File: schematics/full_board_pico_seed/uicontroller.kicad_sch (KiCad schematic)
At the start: 19 parts, among them J5 Conn_02x03_Odd_Even, SW1 Stompbutton 1, SW2 Stompbutton 2, SW3 Stompbutton 3, U5 ATmega88A-A, U6 24LC128

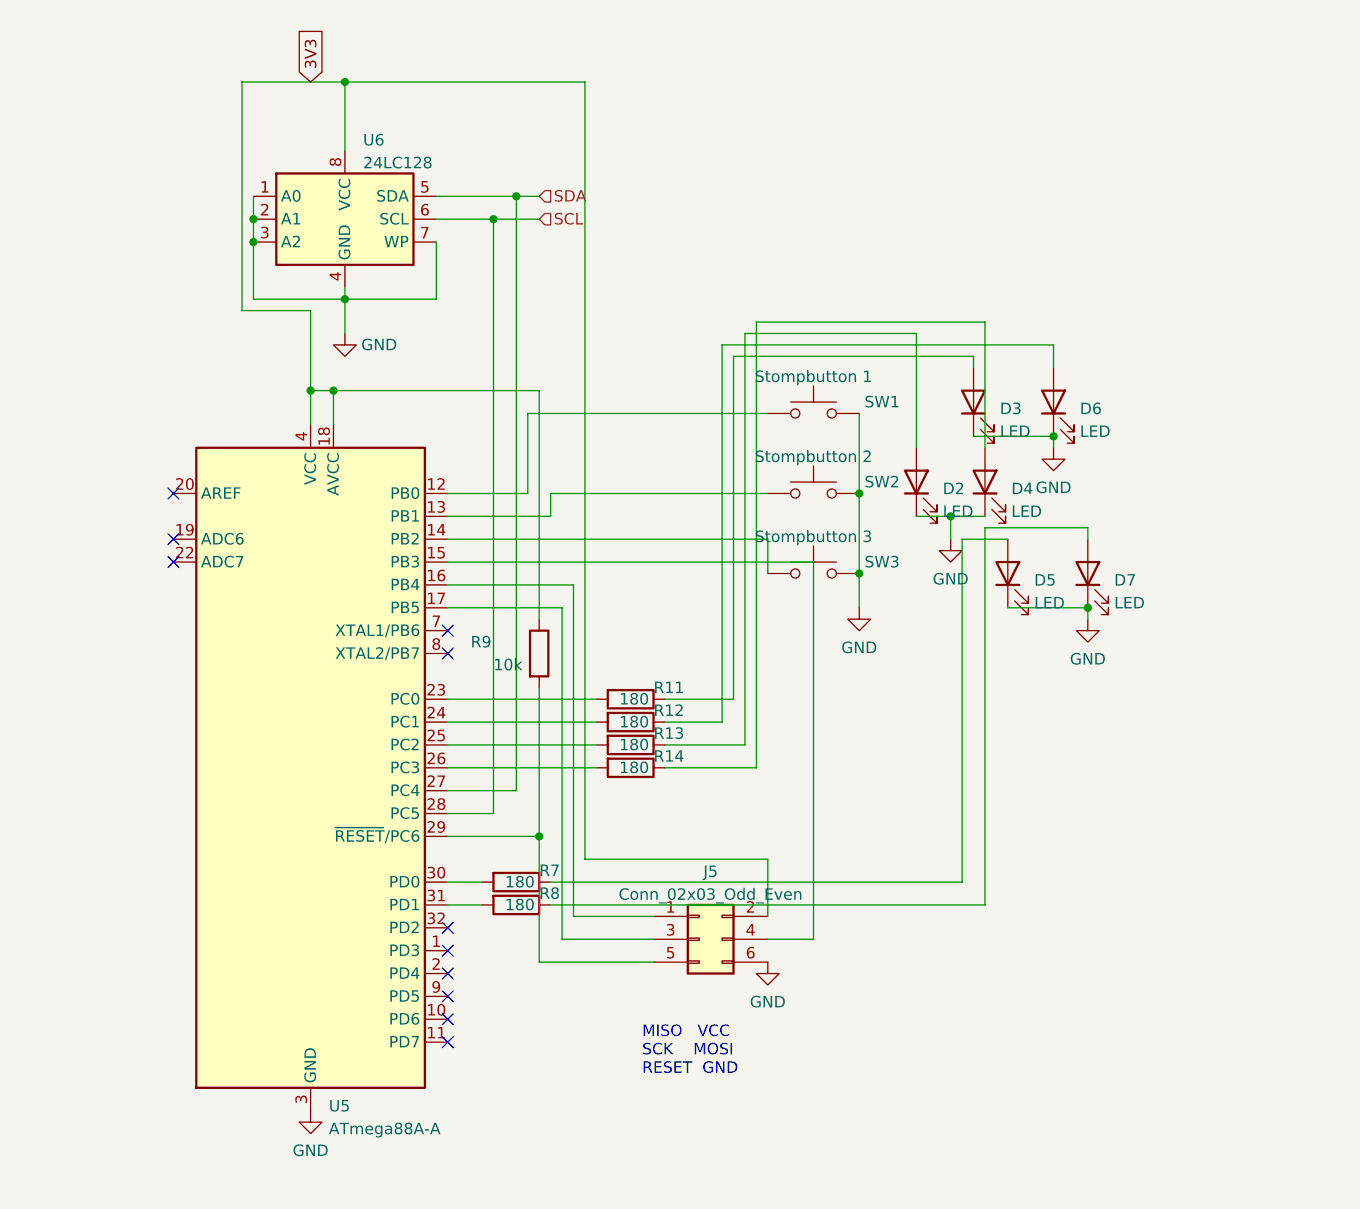
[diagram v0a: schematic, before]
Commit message: added a few testpoints
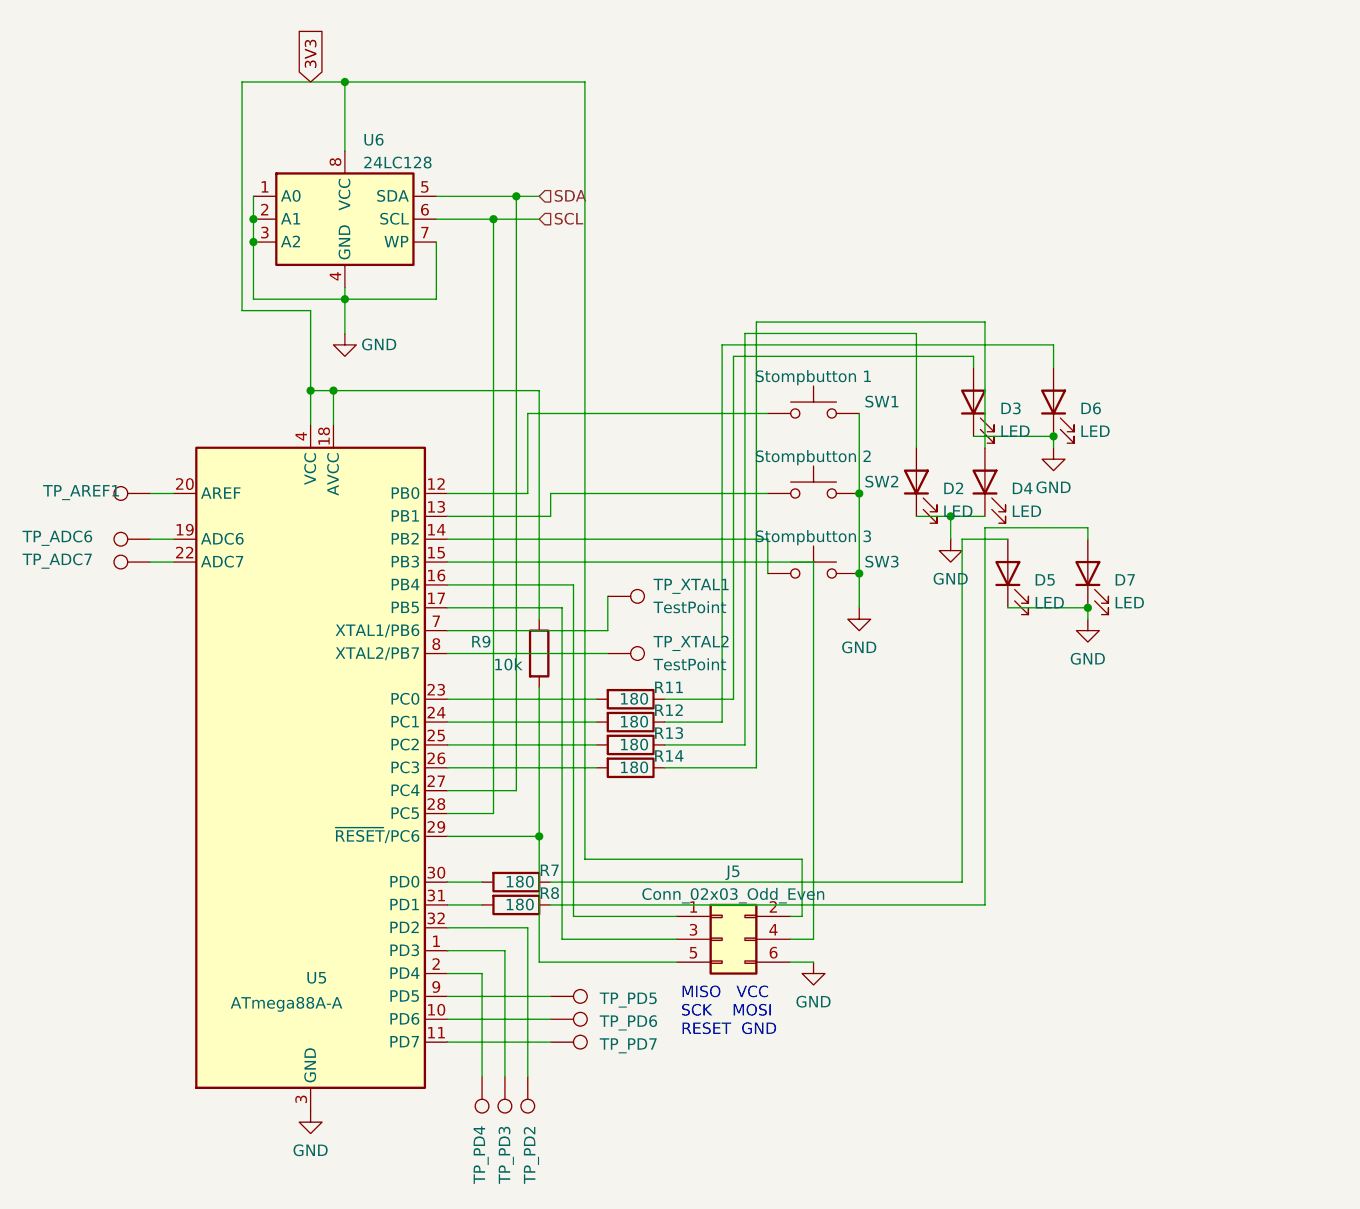
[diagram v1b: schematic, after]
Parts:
- added TP_ADC6, TP_ADC7, TP_AREF1, TP_PD2, TP_PD3, TP_PD4, TP_PD5, TP_PD6, TP_PD7: ~, TestPoint:TestPoint_Pad_D1.5mm, symbol Connector:TestPoint
- added TP_XTAL1, TP_XTAL2: TestPoint, TestPoint:TestPoint_Pad_D1.5mm, symbol Connector:TestPoint
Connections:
- net at U5.1 (PD3): now also TP_PD3.1
- net at U5.10 (PD6): now also TP_PD6.1
- net at U5.11 (PD7): now also TP_PD7.1
- net at U5.19 (ADC6): now also TP_ADC6.1
- net at U5.2 (PD4): now also TP_PD4.1
- net at U5.20 (AREF): now also TP_AREF1.1
- net at U5.22 (ADC7): now also TP_ADC7.1
- net at U5.32 (PD2): now also TP_PD2.1
- net at U5.7 (XTAL1/PB6): now also TP_XTAL1.1
- net at U5.8 (XTAL2/PB7): now also TP_XTAL2.1
- net at U5.9 (PD5): now also TP_PD5.1
- no-connect marks 11 -> 0
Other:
- moved on the sheet: J5

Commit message: worked on schematics
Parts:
- D2, D3, D4, D5, D6, D7, J5, SW1, SW2, SW3, TP_ADC6, TP_ADC7, TP_AREF1, TP_PD2, TP_PD3, TP_PD4, TP_PD5, TP_PD6, TP_PD7, TP_XTAL1, TP_XTAL2: now left out of the parts list
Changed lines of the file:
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@@
 		(shape input)
 		(at 110.49 44.45 0)
-		(fields_autoplaced yes)
 		(effects
 			(font
@@
 		(shape input)
 		(at 110.49 41.91 0)
-		(fields_autoplaced yes)
 		(effects
 			(font
@@
 		(unit 1)
 		(exclude_from_sim no)
-		(in_bom yes)
+		(in_bom no)
 		(on_board yes)
 		(dnp no)
@@
 		(unit 1)
 		(exclude_from_sim no)
-		(in_bom yes)
+		(in_bom no)
 		(on_board yes)
 		(dnp no)
@@
 		(unit 1)
 		(exclude_from_sim no)
-		(in_bom yes)
+		(in_bom no)
 		(on_board yes)
 		(dnp no)
@@
 		(unit 1)
 		(exclude_from_sim no)
-		(in_bom yes)
+		(in_bom no)
 		(on_board yes)
 		(dnp no)
@@
 		(unit 1)
 		(exclude_from_sim no)
-		(in_bom yes)
+		(in_bom no)
 		(on_board yes)
 		(dnp no)
@@
 		(unit 1)
 		(exclude_from_sim no)
-		(in_bom yes)
+		(in_bom no)
 		(on_board yes)
 		(dnp no)
@@
 		(unit 1)
 		(exclude_from_sim no)
-		(in_bom yes)
+		(in_bom no)
 		(on_board yes)
 		(dnp no)
@@
 		(unit 1)
 		(exclude_from_sim no)
-		(in_bom yes)
+		(in_bom no)
 		(on_board yes)
 		(dnp no)
@@
 		(unit 1)
 		(exclude_from_sim no)
-		(in_bom yes)
+		(in_bom no)
 		(on_board yes)
 		(dnp no)
@@
 		(unit 1)
 		(exclude_from_sim no)
-		(in_bom yes)
+		(in_bom no)
 		(on_board yes)
 		(dnp no)
@@
 		(unit 1)
 		(exclude_from_sim no)
-		(in_bom yes)
+		(in_bom no)
 		(on_board yes)
 		(dnp no)
@@
 		(unit 1)
 		(exclude_from_sim no)
-		(in_bom yes)
+		(in_bom no)
 		(on_board yes)
 		(dnp no)
@@
 		(unit 1)
 		(exclude_from_sim no)
-		(in_bom yes)
+		(in_bom no)
 		(on_board yes)
 		(dnp no)
@@
 		(unit 1)
 		(exclude_from_sim no)
-		(in_bom yes)
+		(in_bom no)
 		(on_board yes)
 		(dnp no)
@@
 		(unit 1)
 		(exclude_from_sim no)
-		(in_bom yes)
+		(in_bom no)
 		(on_board yes)
 		(dnp no)
@@
 		(unit 1)
 		(exclude_from_sim no)
-		(in_bom yes)
+		(in_bom no)
 		(on_board yes)
 		(dnp no)
@@
 		(unit 1)
 		(exclude_from_sim no)
-		(in_bom yes)
+		(in_bom no)
 		(on_board yes)
 		(dnp no)
@@
 		(unit 1)
 		(exclude_from_sim no)
-		(in_bom yes)
+		(in_bom no)
 		(on_board yes)
 		(dnp no)
@@
 		(unit 1)
 		(exclude_from_sim no)
-		(in_bom yes)
+		(in_bom no)
 		(on_board yes)
 		(dnp no)
@@
 		(unit 1)
 		(exclude_from_sim no)
-		(in_bom yes)
+		(in_bom no)
 		(on_board yes)
 		(dnp no)
@@
 		(unit 1)
 		(exclude_from_sim no)
-		(in_bom yes)
-		(on_board yes)
-		(dnp no)
+		(in_bom no)
+		(on_board yes)
+		(dnp no)

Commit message: corrected schematic regarding pcm3060
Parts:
- removed D2, D3, D4, D5, D6, D7: LED, Connector_PinHeader_2.54mm:PinHeader_1x02_P2.54mm_Vertical, symbol Device:LED
- added D10, D11, D12: LED_Dual_AAK, LED_THT:LED_D5.0mm-3, symbol Device:LED_Dual_AAK
- renumbered J5 to J10, R13 to R38, R9 to R39, R14 to R40, R7 to R41, R11 to R42, R12 to R43, R8 to R44, TP_AREF1 to TP_AREF, TP_PD5 to TP_PD4, TP_PD7 to TP_PD5, U5 to U7, U6 to U9
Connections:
- net GND: now also D10.3 (K), D11.3 (K), D12.3 (K)
- net at R38.1: now also D10.2 (A2)
- net at R42.1: now also D11.2 (A2)
- net at R43.1: now also D11.1 (A1)
- net at R44.1: now also D12.1 (A1)
- net at R41.1: now also D12.2 (A2)
- net at R40.1: now also D10.1 (A1)

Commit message: schematic change
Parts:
- D2: renamed from D12; now left out of the parts list
- D3: renamed from D11; now left out of the parts list
- D4: renamed from D10; now left out of the parts list
- renumbered R39 to R34, R42 to R35, R43 to R36, R38 to R37, R41 to R38, R40 to R39, R44 to R43, TP_AREF to TP_AREF1, TP_PD4 to TP_PD5, TP_PD5 to TP_PD7
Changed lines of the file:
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@@
 		(unit 1)
 		(exclude_from_sim no)
-		(in_bom yes)
-		(on_board yes)
-		(dnp no)
-		(property "Reference" "D10"
+		(in_bom no)
+		(on_board yes)
+		(dnp no)
+		(property "Reference" "D4"
 			(at 161.29 119.3164 90)
 			(effects
@@
 			(project ""
 				(path "/e63e39d7-6ac0-4ffd-8aa3-1841a4541b55/f9ef1368-05a5-440b-8b6f-d12c6284b642"
-					(reference "D10")
+					(reference "D4")
 					(unit 1)
 				)
@@
 		(on_board yes)
 		(dnp no)
-		(property "Reference" "R38"
+		(property "Reference" "R37"
 			(at 123.19 101.6 90)
 			(effects
@@
 			(project "full_board_pico_seed"
 				(path "/e63e39d7-6ac0-4ffd-8aa3-1841a4541b55/f9ef1368-05a5-440b-8b6f-d12c6284b642"
-					(reference "R38")
+					(reference "R37")
 					(unit 1)
 				)
@@
 		(on_board yes)
 		(dnp no)
-		(property "Reference" "R42"
+		(property "Reference" "R35"
 			(at 123.19 96.52 90)
 			(effects
@@
 			(project "full_board_pico_seed"
 				(path "/e63e39d7-6ac0-4ffd-8aa3-1841a4541b55/f9ef1368-05a5-440b-8b6f-d12c6284b642"
-					(reference "R42")
+					(reference "R35")
 					(unit 1)
 				)
@@
 		(on_board yes)
 		(dnp no)
-		(property "Reference" "R43"
+		(property "Reference" "R36"
 			(at 123.19 99.06 90)
 			(effects
@@
 			(project "full_board_pico_seed"
 				(path "/e63e39d7-6ac0-4ffd-8aa3-1841a4541b55/f9ef1368-05a5-440b-8b6f-d12c6284b642"
-					(reference "R43")
+					(reference "R36")
 					(unit 1)
 				)
@@
 		(on_board yes)
 		(dnp no)
-		(property "Reference" "TP_AREF"
+		(property "Reference" "TP_AREF1"
 			(at 52.578 74.422 90)
 			(effects
@@
 			(project "full_board_pico_seed"
 				(path "/e63e39d7-6ac0-4ffd-8aa3-1841a4541b55/f9ef1368-05a5-440b-8b6f-d12c6284b642"
-					(reference "TP_AREF")
+					(reference "TP_AREF1")
 					(unit 1)
 				)
@@
 		(on_board yes)
 		(dnp no)
-		(property "Reference" "R44"
+		(property "Reference" "R43"
 			(at 110.49 119.38 90)
 			(effects
@@
 			(project "full_board_pico_seed"
 				(path "/e63e39d7-6ac0-4ffd-8aa3-1841a4541b55/f9ef1368-05a5-440b-8b6f-d12c6284b642"
-					(reference "R44")
+					(reference "R43")
 					(unit 1)
 				)
@@
 		(unit 1)
 		(exclude_from_sim no)
-		(in_bom yes)
+		(in_bom no)
 		(on_board yes)
 		(dnp no)
 		(fields_autoplaced yes)
-		(property "Reference" "D12"
+		(property "Reference" "D2"
 			(at 177.8 129.4764 90)
 			(effects
@@
 			(project ""
 				(path "/e63e39d7-6ac0-4ffd-8aa3-1841a4541b55/f9ef1368-05a5-440b-8b6f-d12c6284b642"
-					(reference "D12")
+					(reference "D2")
 					(unit 1)
 				)
@@
 		(on_board yes)
 		(dnp no)
-		(property "Reference" "R41"
+		(property "Reference" "R38"
 			(at 110.49 116.84 90)
 			(effects
@@
 			(project "full_board_pico_seed"
 				(path "/e63e39d7-6ac0-4ffd-8aa3-1841a4541b55/f9ef1368-05a5-440b-8b6f-d12c6284b642"
-					(reference "R41")
+					(reference "R38")
 					(unit 1)
 				)
@@
 		(on_board yes)
 		(dnp no)
-		(property "Reference" "TP_PD4"
+		(property "Reference" "TP_PD5"
 			(at 123.698 131.064 90)
 			(effects
@@
 			(project "full_board_pico_seed"
 				(path "/e63e39d7-6ac0-4ffd-8aa3-1841a4541b55/f9ef1368-05a5-440b-8b6f-d12c6284b642"
-					(reference "TP_PD4")
+					(reference "TP_PD5")
 					(unit 1)
 				)
@@
 		(on_board yes)
 		(dnp no)
-		(property "Reference" "R39"
+		(property "Reference" "R34"
 			(at 102.87 91.44 0)
 			(effects
@@
 			(project "full_board_pico_seed"
 				(path "/e63e39d7-6ac0-4ffd-8aa3-1841a4541b55/f9ef1368-05a5-440b-8b6f-d12c6284b642"
-					(reference "R39")
+					(reference "R34")
 					(unit 1)
 				)
@@
 		(unit 1)
 		(exclude_from_sim no)
-		(in_bom yes)
+		(in_bom no)
 		(on_board yes)
 		(dnp no)
 		(fields_autoplaced yes)
-		(property "Reference" "D11"
+		(property "Reference" "D3"
 			(at 184.15 107.8864 90)
 			(effects
@@
 			(project ""
 				(path "/e63e39d7-6ac0-4ffd-8aa3-1841a4541b55/f9ef1368-05a5-440b-8b6f-d12c6284b642"
-					(reference "D11")
+					(reference "D3")
 					(unit 1)
 				)
@@
 		(on_board yes)
 		(dnp no)
-		(property "Reference" "R40"
+		(property "Reference" "R39"
 			(at 123.19 104.14 90)
 			(effects
@@
 			(project "full_board_pico_seed"
 				(path "/e63e39d7-6ac0-4ffd-8aa3-1841a4541b55/f9ef1368-05a5-440b-8b6f-d12c6284b642"
-					(reference "R40")
+					(reference "R39")
 					(unit 1)
 				)
@@
 		(on_board yes)
 		(dnp no)
-		(property "Reference" "TP_PD5"
+		(property "Reference" "TP_PD7"
 			(at 123.698 136.144 90)
 			(effects
@@
 			(project "full_board_pico_seed"
 				(path "/e63e39d7-6ac0-4ffd-8aa3-1841a4541b55/f9ef1368-05a5-440b-8b6f-d12c6284b642"
-					(reference "TP_PD5")
-					(unit 1)
-				)
+					(reference "TP_PD7")
+					(unit 1)
+				)

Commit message: updated schematic
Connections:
- net prog_mosi: now reaches J10.4 (Pin_4), U7.15 (PB3)
- net prog_miso: now reaches J10.1 (Pin_1), U7.16 (PB4)
- net prog_sck: now reaches J10.3 (Pin_3), U7.17 (PB5)
- net prog_reset: now reaches J10.5 (Pin_5), R34.2, U7.29 (~{RESET}/PC6)
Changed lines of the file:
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@@
+	)
+	(junction
+		(at 124.46 121.92)
+		(diameter 0)
+		(color 0 0 0 0)
 	)
 	(junction
@@
 	)
 	(junction
+		(at 120.65 127)
+		(diameter 0)
+		(color 0 0 0 0)
+	)
+	(junction
 		(at 107.95 41.91)
 		(diameter 0)
@@
 	)
 	(junction
+		(at 140.97 124.46)
+		(diameter 0)
+		(color 0 0 0 0)
+	)
+	(junction
+		(at 123.19 124.46)
+		(diameter 0)
+		(color 0 0 0 0)
+	)
+	(junction
 		(at 105.41 44.45)
 		(diameter 0)
@@
 	(wire
 		(pts
-			(xy 125.73 127) (xy 110.49 127)
+			(xy 146.05 137.16) (xy 146.05 124.46)
+		)
+		(stroke
+			(width 0)
+			(type default)
+		)
+	)
+	(wire
+		(pts
+			(xy 125.73 127) (xy 120.65 127)
 		)
 		(stroke
@@
 	(wire
 		(pts
-			(xy 113.03 124.46) (xy 125.73 124.46)
+			(xy 113.03 124.46) (xy 123.19 124.46)
 		)
 		(stroke
@@
 	(wire
 		(pts
+			(xy 120.65 127) (xy 110.49 127)
+		)
+		(stroke
+			(width 0)
+			(type default)
+		)
+	)
+	(wire
+		(pts
+			(xy 123.19 124.46) (xy 125.73 124.46)
+		)
+		(stroke
+			(width 0)
+			(type default)
+		)
+	)
+	(wire
+		(pts
 			(xy 114.3 85.09) (xy 114.3 121.92)
 		)
@@
 	(wire
 		(pts
-			(xy 114.3 121.92) (xy 125.73 121.92)
+			(xy 114.3 121.92) (xy 124.46 121.92)
 		)
 		(stroke
@@
 	(wire
 		(pts
+			(xy 134.62 137.16) (xy 146.05 137.16)
+		)
+		(stroke
+			(width 0)
+			(type default)
+		)
+	)
+	(wire
+		(pts
 			(xy 146.05 87.63) (xy 146.05 83.82)
 		)
@@
 	(wire
 		(pts
+			(xy 123.19 147.32) (xy 123.19 124.46)
+		)
+		(stroke
+			(width 0)
+			(type default)
+		)
+	)
+	(wire
+		(pts
 			(xy 105.41 110.49) (xy 105.41 44.45)
 		)
@@
 	(wire
 		(pts
+			(xy 134.62 143.51) (xy 134.62 137.16)
+		)
+		(stroke
+			(width 0)
+			(type default)
+		)
+	)
+	(wire
+		(pts
 			(xy 87.63 63.5) (xy 85.09 63.5)
 		)
@@
 	(wire
 		(pts
+			(xy 124.46 121.92) (xy 125.73 121.92)
+		)
+		(stroke
+			(width 0)
+			(type default)
+		)
+	)
+	(wire
+		(pts
 			(xy 109.22 66.04) (xy 135.89 66.04)
 		)
@@
 	(wire
 		(pts
+			(xy 124.46 139.7) (xy 124.46 121.92)
+		)
+		(stroke
+			(width 0)
+			(type default)
+		)
+	)
+	(wire
+		(pts
 			(xy 124.46 105.41) (xy 152.4 105.41)
 		)
@@
 	(wire
 		(pts
+			(xy 137.16 147.32) (xy 123.19 147.32)
+		)
+		(stroke
+			(width 0)
+			(type default)
+		)
+	)
+	(wire
+		(pts
 			(xy 77.47 29.21) (xy 88.9 29.21)
 		)
@@
 	(wire
 		(pts
+			(xy 135.89 139.7) (xy 124.46 139.7)
+		)
+		(stroke
+			(width 0)
+			(type default)
+		)
+	)
+	(wire
+		(pts
 			(xy 105.41 44.45) (xy 99.06 44.45)
 		)
@@
 	(wire
 		(pts
+			(xy 135.89 143.51) (xy 134.62 143.51)
+		)
+		(stroke
+			(width 0)
+			(type default)
+		)
+	)
+	(wire
+		(pts
 			(xy 168.91 120.65) (xy 168.91 123.19)
 		)
@@
 	(wire
 		(pts
+			(xy 120.65 151.13) (xy 120.65 127)
+		)
+		(stroke
+			(width 0)
+			(type default)
+		)
+	)
+	(wire
+		(pts
 			(xy 100.33 100.33) (xy 116.84 100.33)
 		)
@@
 		(pts
 			(xy 171.45 138.43) (xy 171.45 139.7)
+		)
+		(stroke
+			(width 0)
+			(type default)
+		)
+	)
+	(wire
+		(pts
+			(xy 135.89 151.13) (xy 120.65 151.13)
+		)
+		(stroke
+			(width 0)
+			(type default)
+		)
+	)
+	(wire
+		(pts
+			(xy 146.05 124.46) (xy 140.97 124.46)
 		)
 		(stroke
@@
 		)
 	)
+	(hierarchical_label "prog_miso"
+		(shape input)
+		(at 135.89 139.7 0)
+		(effects
+			(font
+				(size 1.27 1.27)
+			)
+			(justify left)
+		)
+	)
+	(hierarchical_label "prog_mosi"
+		(shape input)
+		(at 135.89 143.51 0)
+		(effects
+			(font
+				(size 1.27 1.27)
+			)
+			(justify left)
+		)
+	)
 	(hierarchical_label "SCL"
 		(shape input)
@@
 		(effects
 			(font
+				(size 1.27 1.27)
+			)
+			(justify left)
+		)
+	)
+	(hierarchical_label "prog_reset"
+		(shape input)
+		(at 135.89 151.13 0)
+		(effects
+			(font
+				(size 1.27 1.27)
+			)
+			(justify left)
+		)
+	)
+	(hierarchical_label "prog_sck"
+		(shape input)
+		(at 137.16 147.32 0)
+		(effects
+			(font
